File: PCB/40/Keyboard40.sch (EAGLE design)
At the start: 118 parts, among them J1 UX60SC-MB-5S8, SW1 TL3342F160QG/TR, U1 ATMEGA32U4-AUR, X1 FA-238

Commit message: Output files for 40
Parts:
- C6: value 4.7uF -> 1uF
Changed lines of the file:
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@@
 <part name="X1" library="FA-238" deviceset="FA-238" device=""/>
 <part name="P+1" library="supply1" library_urn="urn:adsk.eagle:library:371" deviceset="VCC" device=""/>
-<part name="GND2" library="supply1" library_urn="urn:adsk.eagle:library:371" deviceset="GND" device=""/>
 <part name="C1" library="rcl" library_urn="urn:adsk.eagle:library:334" deviceset="C-US" device="C0805" package3d_urn="urn:adsk.eagle:package:23617/2" value=".1uF"/>
 <part name="C2" library="rcl" library_urn="urn:adsk.eagle:library:334" deviceset="C-US" device="C0805" package3d_urn="urn:adsk.eagle:package:23617/2" value=".1uF"/>
@@
 <part name="R7" library="rcl" library_urn="urn:adsk.eagle:library:334" deviceset="R-US_" device="R0805" package3d_urn="urn:adsk.eagle:package:23553/2" value="22"/>
 <part name="R8" library="rcl" library_urn="urn:adsk.eagle:library:334" deviceset="R-US_" device="R0805" package3d_urn="urn:adsk.eagle:package:23553/2" value="22"/>
-<part name="C6" library="rcl" library_urn="urn:adsk.eagle:library:334" deviceset="C-US" device="C0805" package3d_urn="urn:adsk.eagle:package:23617/2" value="4.7uF"/>
+<part name="C6" library="rcl" library_urn="urn:adsk.eagle:library:334" deviceset="C-US" device="C0805" package3d_urn="urn:adsk.eagle:package:23617/2" value="1uF"/>
 <part name="GND6" library="supply1" library_urn="urn:adsk.eagle:library:371" deviceset="GND" device=""/>
 <part name="D16" library="BAV21W-7-F" deviceset="BAV21W-7-F" device=""/>
@@
 <attribute name="VALUE" x="137.16" y="22.86" size="1.778" layer="96" rot="R90"/>
 </instance>
-<instance part="GND2" gate="1" x="139.7" y="2.54" smashed="yes">
-<attribute name="VALUE" x="137.16" y="0" size="1.778" layer="96"/>
-</instance>
 <instance part="C1" gate="G$1" x="139.7" y="15.24" smashed="yes">
 <attribute name="NAME" x="140.716" y="15.875" size="1.778" layer="95"/>
@@
 <nets>
 <net name="GND" class="0">
-<segment>
-<pinref part="C1" gate="G$1" pin="2"/>
-<pinref part="GND2" gate="1" pin="GND"/>
-<wire x1="139.7" y1="10.16" x2="139.7" y2="7.62" width="0.1524" layer="91"/>
-<wire x1="139.7" y1="7.62" x2="139.7" y2="5.08" width="0.1524" layer="91"/>
-<wire x1="139.7" y1="7.62" x2="149.86" y2="7.62" width="0.1524" layer="91"/>
-<junction x="139.7" y="7.62"/>
-<pinref part="C2" gate="G$1" pin="2"/>
-<wire x1="149.86" y1="7.62" x2="149.86" y2="10.16" width="0.1524" layer="91"/>
-<wire x1="149.86" y1="7.62" x2="160.02" y2="7.62" width="0.1524" layer="91"/>
-<junction x="149.86" y="7.62"/>
-<pinref part="C3" gate="G$1" pin="2"/>
-<wire x1="160.02" y1="7.62" x2="160.02" y2="10.16" width="0.1524" layer="91"/>
-<wire x1="160.02" y1="7.62" x2="170.18" y2="7.62" width="0.1524" layer="91"/>
-<junction x="160.02" y="7.62"/>
-<pinref part="C4" gate="G$1" pin="2"/>
-<wire x1="170.18" y1="7.62" x2="170.18" y2="10.16" width="0.1524" layer="91"/>
-<wire x1="170.18" y1="7.62" x2="180.34" y2="7.62" width="0.1524" layer="91"/>
-<junction x="170.18" y="7.62"/>
-<pinref part="C5" gate="G$1" pin="2"/>
-<wire x1="180.34" y1="7.62" x2="180.34" y2="10.16" width="0.1524" layer="91"/>
-<pinref part="GND3" gate="1" pin="GND"/>
-<junction x="139.7" y="5.08"/>
-</segment>
 <segment>
 <pinref part="GND4" gate="1" pin="GND"/>
@@
 <pinref part="GND9" gate="1" pin="GND"/>
 </segment>
+<segment>
+<pinref part="C1" gate="G$1" pin="2"/>
+<wire x1="139.7" y1="10.16" x2="139.7" y2="7.62" width="0.1524" layer="91"/>
+<wire x1="139.7" y1="7.62" x2="149.86" y2="7.62" width="0.1524" layer="91"/>
+<pinref part="C2" gate="G$1" pin="2"/>
+<wire x1="149.86" y1="7.62" x2="149.86" y2="10.16" width="0.1524" layer="91"/>
+<wire x1="149.86" y1="7.62" x2="160.02" y2="7.62" width="0.1524" layer="91"/>
+<junction x="149.86" y="7.62"/>
+<pinref part="C3" gate="G$1" pin="2"/>
+<wire x1="160.02" y1="7.62" x2="160.02" y2="10.16" width="0.1524" layer="91"/>
+<wire x1="160.02" y1="7.62" x2="170.18" y2="7.62" width="0.1524" layer="91"/>
+<junction x="160.02" y="7.62"/>
+<pinref part="C4" gate="G$1" pin="2"/>
+<wire x1="170.18" y1="7.62" x2="170.18" y2="10.16" width="0.1524" layer="91"/>
+<wire x1="170.18" y1="7.62" x2="180.34" y2="7.62" width="0.1524" layer="91"/>
+<junction x="170.18" y="7.62"/>
+<pinref part="C5" gate="G$1" pin="2"/>
+<wire x1="180.34" y1="7.62" x2="180.34" y2="10.16" width="0.1524" layer="91"/>
+<pinref part="GND3" gate="1" pin="GND"/>
+<wire x1="139.7" y1="5.08" x2="139.7" y2="7.62" width="0.1524" layer="91"/>
+<junction x="139.7" y="7.62"/>
+</segment>
 </net>

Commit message: Cleanup. Add holes and use plate switches
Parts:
- U$1, U$10, U$11, U$12, U$16, U$17, U$18, U$19, U$2, U$20, U$21, U$22, U$23, U$24, U$25, U$26, U$27, U$28, U$29, U$3, U$30, U$31, U$32, U$33, U$34, U$35, U$36, U$37, U$38, U$39, U$4, U$40, U$41, U$42, U$43, U$44, U$45, U$46, U$47, U$48, U$49, U$5, U$50, U$51, U$6, U$7, U$8, U$9: value CHERRY_MX -> CHERRY_MXCHERRY_MX_PLATE; device CHERRY_MX:CHERRY_MX -> CHERRY_MX:CHERRY_MXCHERRY_MX_PLATE
- U$13, U$14, U$15: value CHERRY_MXCHERRY_MX_1_2 -> CHERRY_MXCHERRY_MX_1_2_PLATE; device CHERRY_MX:CHERRY_MXCHERRY_MX_1_2 -> CHERRY_MX:CHERRY_MXCHERRY_MX_1_2_PLATE

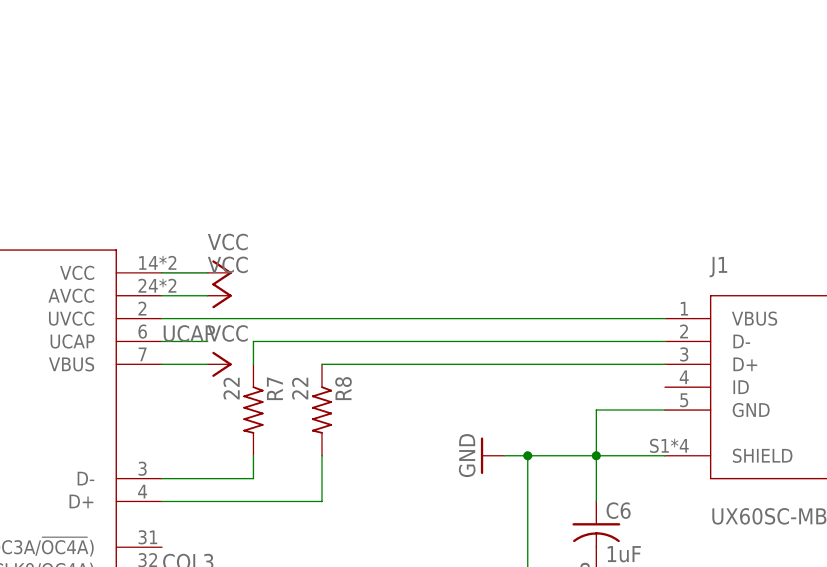
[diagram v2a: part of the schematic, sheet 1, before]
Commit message: VUSB to VCC. Fix USB position
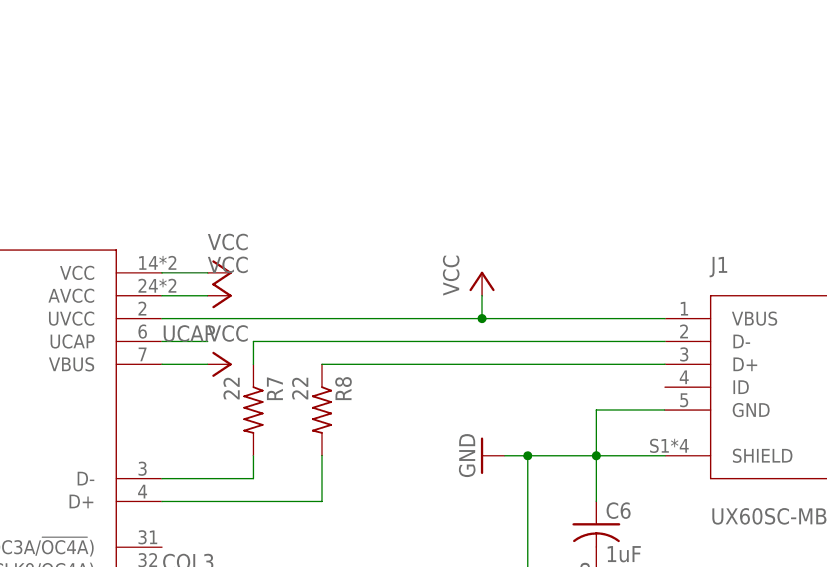
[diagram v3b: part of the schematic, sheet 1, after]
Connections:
- removed net N$13: J1.VBUS, U1.UVCC
- net VCC: now also J1.VBUS, U1.UVCC
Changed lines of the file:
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@@
 <part name="D50" library="BAV21W-7-F" deviceset="BAV21W-7-F" device=""/>
 <part name="D51" library="BAV21W-7-F" deviceset="BAV21W-7-F" device=""/>
+<part name="P+6" library="supply1" library_urn="urn:adsk.eagle:library:371" deviceset="VCC" device=""/>
 </parts>
 <sheets>
@@
 <instance part="P+5" gate="VCC" x="271.78" y="106.68" smashed="yes" rot="R270">
 <attribute name="VALUE" x="269.24" y="109.22" size="1.778" layer="96"/>
+</instance>
+<instance part="P+6" gate="VCC" x="299.72" y="116.84" smashed="yes">
+<attribute name="VALUE" x="297.18" y="114.3" size="1.778" layer="96" rot="R90"/>
 </instance>
 </instances>
@@
 <pinref part="P+5" gate="VCC" pin="VCC"/>
 </segment>
+<segment>
+<pinref part="U1" gate="G$1" pin="UVCC"/>
+<wire x1="264.16" y1="111.76" x2="299.72" y2="111.76" width="0.1524" layer="91"/>
+<pinref part="J1" gate="G$1" pin="VBUS"/>
+<wire x1="299.72" y1="111.76" x2="320.04" y2="111.76" width="0.1524" layer="91"/>
+<wire x1="299.72" y1="111.76" x2="299.72" y2="114.3" width="0.1524" layer="91"/>
+<junction x="299.72" y="111.76"/>
+<pinref part="P+6" gate="VCC" pin="VCC"/>
+</segment>
 </net>
 <net name="N$9" class="0">
@@
 </segment>
 </net>
-<net name="N$13" class="0">
-<segment>
-<pinref part="U1" gate="G$1" pin="UVCC"/>
-<wire x1="264.16" y1="111.76" x2="320.04" y2="111.76" width="0.1524" layer="91"/>
-<pinref part="J1" gate="G$1" pin="VBUS"/>
-</segment>
-</net>
